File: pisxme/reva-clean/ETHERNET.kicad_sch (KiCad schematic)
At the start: 3 parts

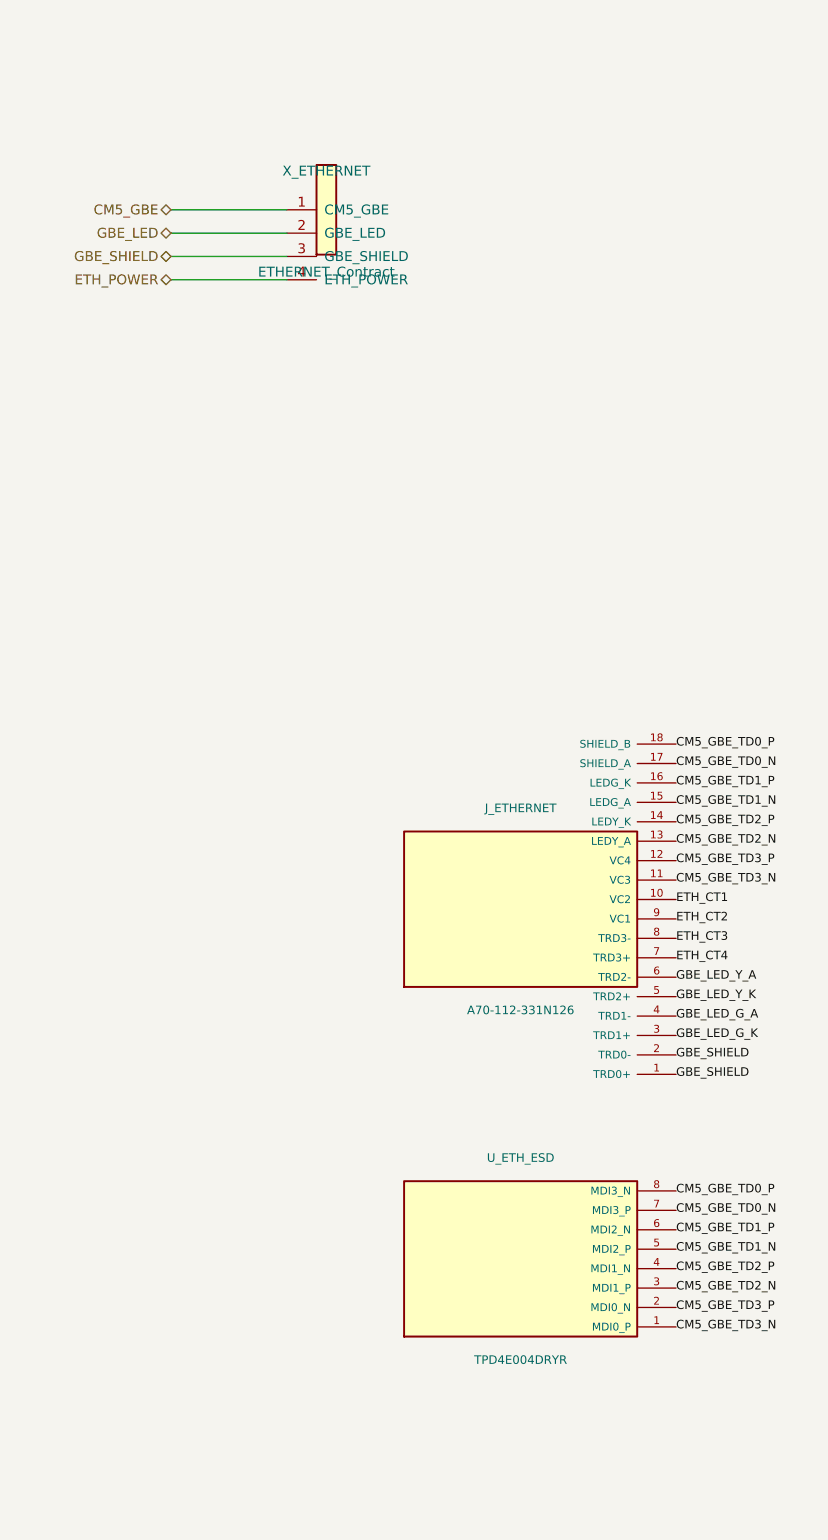
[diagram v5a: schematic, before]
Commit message: fix KiCad annotation and netlist export
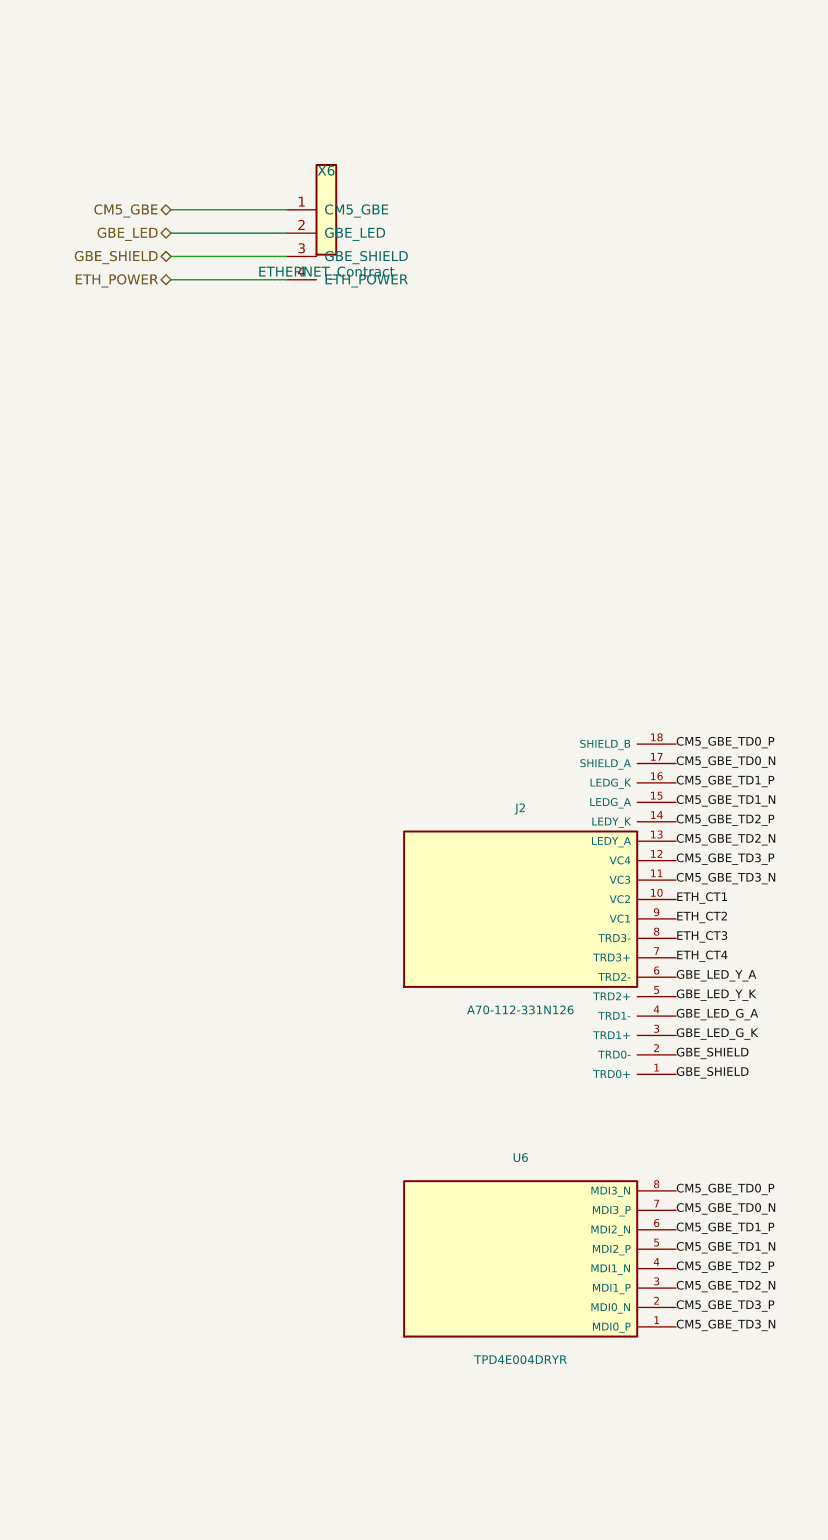
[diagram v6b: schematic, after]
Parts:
- renumbered J_ETHERNET to J2, U_ETH_ESD to U6, X_ETHERNET to X6
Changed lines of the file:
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@@
     (on_board no)
     (dnp no)
-    (property "Reference" "X_ETHERNET"
+    (property "Reference" "X6"
       (at 25 5 0)
       (effects (font (size 1.27 1.27))))
@@
     (pin "4")
     (instances (project "PiSXMe_RevA_Clean"
-      (path "/30000000-0000-0000-0000-000000000000/10000000-0000-0000-0000-000000000006" (reference "X_ETHERNET" ) (unit 1))))
+      (path "/30000000-0000-0000-0000-000000000000/10000000-0000-0000-0000-000000000006" (reference "X6" ) (unit 1))))
   )
 (label "CM5_GBE_TD0_P" (at 70 78.75 0) (effects (font (size 1.1 1.1)) (justify left)))
@@
 (label "GBE_SHIELD" (at 70 118.75 0) (effects (font (size 1.1 1.1)) (justify left)))
 (label "GBE_SHIELD" (at 70 121.25 0) (effects (font (size 1.1 1.1)) (justify left)))
-(symbol (lib_id "PiSXMeRevAClean:EDAC_A70_112_331N126_Ethernet") (at 50 100 0) (unit 1) (exclude_from_sim no) (in_bom yes) (on_board yes) (dnp no) (property "Reference" "J_ETHERNET" (at 50 87 0) (effects (font (size 1.1 1.1)))) (property "Value" "A70-112-331N126" (at 50 113 0) (effects (font (size 1.1 1.1)))) (property "MPN" "A70-112-331N126" (at 50 100 0) (effects (font (size 1 1)) (hide yes))) (property "Footprint" "PiSXMeRevAClean:EDAC_A70_112_331N126" (at 50 100 0) (effects (font (size 1 1)) (hide yes))) (pin "1")
+(symbol (lib_id "PiSXMeRevAClean:EDAC_A70_112_331N126_Ethernet") (at 50 100 0) (unit 1) (exclude_from_sim no) (in_bom yes) (on_board yes) (dnp no) (property "Reference" "J2" (at 50 87 0) (effects (font (size 1.1 1.1)))) (property "Value" "A70-112-331N126" (at 50 113 0) (effects (font (size 1.1 1.1)))) (property "MPN" "A70-112-331N126" (at 50 100 0) (effects (font (size 1 1)) (hide yes))) (property "Footprint" "PiSXMeRevAClean:EDAC_A70_112_331N126" (at 50 100 0) (effects (font (size 1 1)) (hide yes))) (pin "1")
 (pin "2")
 (pin "3")
@@
 (pin "16")
 (pin "17")
-(pin "18") (instances (project "PiSXMe_RevA_Clean" (path "/30000000-0000-0000-0000-000000000000" (reference "J_ETHERNET") (unit 1)))) )(label "CM5_GBE_TD0_P" (at 70 136.25 0) (effects (font (size 1.1 1.1)) (justify left)))
+(pin "18") (instances (project "PiSXMe_RevA_Clean" (path "/30000000-0000-0000-0000-000000000000" (reference "J2") (unit 1)))) )(label "CM5_GBE_TD0_P" (at 70 136.25 0) (effects (font (size 1.1 1.1)) (justify left)))
 (label "CM5_GBE_TD0_N" (at 70 138.75 0) (effects (font (size 1.1 1.1)) (justify left)))
 (label "CM5_GBE_TD1_P" (at 70 141.25 0) (effects (font (size 1.1 1.1)) (justify left)))
@@
 (label "CM5_GBE_TD3_P" (at 70 151.25 0) (effects (font (size 1.1 1.1)) (justify left)))
 (label "CM5_GBE_TD3_N" (at 70 153.75 0) (effects (font (size 1.1 1.1)) (justify left)))
-(symbol (lib_id "PiSXMeRevAClean:TPD4E004DRYR") (at 50 145 0) (unit 1) (exclude_from_sim no) (in_bom yes) (on_board yes) (dnp no) (property "Reference" "U_ETH_ESD" (at 50 132 0) (effects (font (size 1.1 1.1)))) (property "Value" "TPD4E004DRYR" (at 50 158 0) (effects (font (size 1.1 1.1)))) (property "MPN" "TPD4E004DRYR" (at 50 145 0) (effects (font (size 1 1)) (hide yes))) (property "Footprint" "PiSXMeRevAClean:TPD4E004DRYR_WSON6" (at 50 145 0) (effects (font (size 1 1)) (hide yes))) (pin "1")
+(symbol (lib_id "PiSXMeRevAClean:TPD4E004DRYR") (at 50 145 0) (unit 1) (exclude_from_sim no) (in_bom yes) (on_board yes) (dnp no) (property "Reference" "U6" (at 50 132 0) (effects (font (size 1.1 1.1)))) (property "Value" "TPD4E004DRYR" (at 50 158 0) (effects (font (size 1.1 1.1)))) (property "MPN" "TPD4E004DRYR" (at 50 145 0) (effects (font (size 1 1)) (hide yes))) (property "Footprint" "PiSXMeRevAClean:TPD4E004DRYR_WSON6" (at 50 145 0) (effects (font (size 1 1)) (hide yes))) (pin "1")
 (pin "2")
 (pin "3")
@@
 (pin "6")
 (pin "7")
-(pin "8") (instances (project "PiSXMe_RevA_Clean" (path "/30000000-0000-0000-0000-000000000000" (reference "U_ETH_ESD") (unit 1)))) )
+(pin "8") (instances (project "PiSXMe_RevA_Clean" (path "/30000000-0000-0000-0000-000000000000" (reference "U6") (unit 1)))) )
   (sheet_instances (path "/30000000-0000-0000-0000-000000000000/10000000-0000-0000-0000-000000000006" (page "6")))
 )

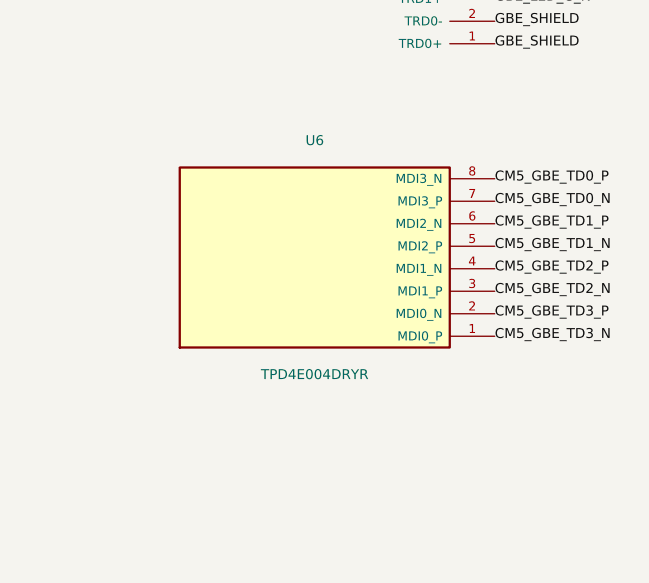
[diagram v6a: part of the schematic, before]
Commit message: correct Ethernet ESD and regulator authority
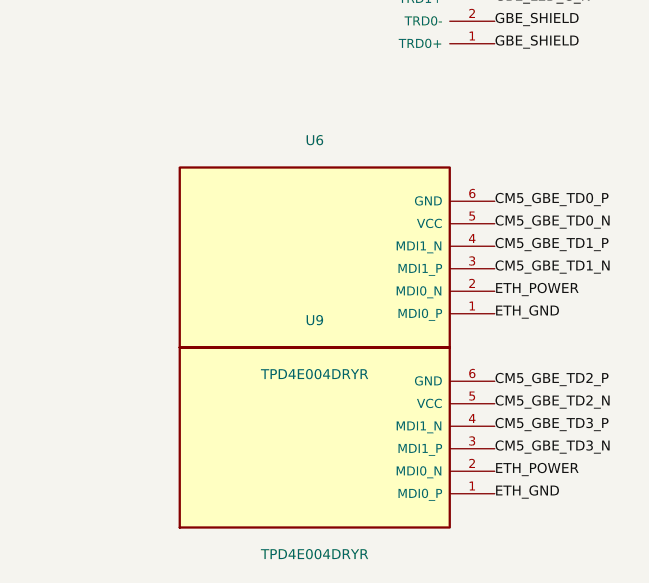
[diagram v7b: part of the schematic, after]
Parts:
- added U9: TPD4E004DRYR, PiSXMeRevAClean:TPD4E004DRYR_WSON6, symbol PiSXMeRevAClean:TPD4E004DRYR
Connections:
- net CM5_GBE_TD0_N: now also U6.5 (VCC); no longer U6.7 (MDI3_P)
- net CM5_GBE_TD0_P: now also U6.6 (GND); no longer U6.8 (MDI3_N)
- net CM5_GBE_TD1_N: now also U6.3 (MDI1_P); no longer U6.5 (MDI2_P)
- net CM5_GBE_TD1_P: now also U6.4 (MDI1_N); no longer U6.6 (MDI2_N)
- net CM5_GBE_TD2_N: now also U9.5 (VCC); no longer U6.3 (MDI1_P)
- net CM5_GBE_TD2_P: now also U9.6 (GND); no longer U6.4 (MDI1_N)
- net CM5_GBE_TD3_N: now also U9.3 (MDI1_P); no longer U6.1 (MDI0_P)
- net CM5_GBE_TD3_P: now also U9.4 (MDI1_N); no longer U6.2 (MDI0_N)
- net ETH_POWER: now also U6.2 (MDI0_N), U9.2 (MDI0_N)
- new net ETH_GND: U6.1 (MDI0_P), U9.1 (MDI0_P)
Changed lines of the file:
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@@
 (pin "16")
 (pin "17")
-(pin "18") (instances (project "PiSXMe_RevA_Clean" (path "/30000000-0000-0000-0000-000000000000" (reference "J2") (unit 1)))) )(label "CM5_GBE_TD0_P" (at 70 136.25 0) (effects (font (size 1.1 1.1)) (justify left)))
-(label "CM5_GBE_TD0_N" (at 70 138.75 0) (effects (font (size 1.1 1.1)) (justify left)))
-(label "CM5_GBE_TD1_P" (at 70 141.25 0) (effects (font (size 1.1 1.1)) (justify left)))
-(label "CM5_GBE_TD1_N" (at 70 143.75 0) (effects (font (size 1.1 1.1)) (justify left)))
-(label "CM5_GBE_TD2_P" (at 70 146.25 0) (effects (font (size 1.1 1.1)) (justify left)))
-(label "CM5_GBE_TD2_N" (at 70 148.75 0) (effects (font (size 1.1 1.1)) (justify left)))
-(label "CM5_GBE_TD3_P" (at 70 151.25 0) (effects (font (size 1.1 1.1)) (justify left)))
-(label "CM5_GBE_TD3_N" (at 70 153.75 0) (effects (font (size 1.1 1.1)) (justify left)))
+(pin "18") (instances (project "PiSXMe_RevA_Clean" (path "/30000000-0000-0000-0000-000000000000" (reference "J2") (unit 1)))) )
+(label "CM5_GBE_TD0_P" (at 70 138.75 0) (effects (font (size 1.1 1.1)) (justify left)))
+(label "CM5_GBE_TD0_N" (at 70 141.25 0) (effects (font (size 1.1 1.1)) (justify left)))
+(label "CM5_GBE_TD1_P" (at 70 143.75 0) (effects (font (size 1.1 1.1)) (justify left)))
+(label "CM5_GBE_TD1_N" (at 70 146.25 0) (effects (font (size 1.1 1.1)) (justify left)))
+(label "ETH_POWER" (at 70 148.75 0) (effects (font (size 1.1 1.1)) (justify left)))
+(label "ETH_GND" (at 70 151.25 0) (effects (font (size 1.1 1.1)) (justify left)))
 (symbol (lib_id "PiSXMeRevAClean:TPD4E004DRYR") (at 50 145 0) (unit 1) (exclude_from_sim no) (in_bom yes) (on_board yes) (dnp no) (property "Reference" "U6" (at 50 132 0) (effects (font (size 1.1 1.1)))) (property "Value" "TPD4E004DRYR" (at 50 158 0) (effects (font (size 1.1 1.1)))) (property "MPN" "TPD4E004DRYR" (at 50 145 0) (effects (font (size 1 1)) (hide yes))) (property "Footprint" "PiSXMeRevAClean:TPD4E004DRYR_WSON6" (at 50 145 0) (effects (font (size 1 1)) (hide yes))) (pin "1")
 (pin "2")
@@
 (pin "4")
 (pin "5")
-(pin "6")
-(pin "7")
-(pin "8") (instances (project "PiSXMe_RevA_Clean" (path "/30000000-0000-0000-0000-000000000000" (reference "U6") (unit 1)))) )
+(pin "6") (instances (project "PiSXMe_RevA_Clean" (path "/30000000-0000-0000-0000-000000000000" (reference "U6") (unit 1)))) )(label "CM5_GBE_TD2_P" (at 70 158.75 0) (effects (font (size 1.1 1.1)) (justify left)))
+(label "CM5_GBE_TD2_N" (at 70 161.25 0) (effects (font (size 1.1 1.1)) (justify left)))
+(label "CM5_GBE_TD3_P" (at 70 163.75 0) (effects (font (size 1.1 1.1)) (justify left)))
+(label "CM5_GBE_TD3_N" (at 70 166.25 0) (effects (font (size 1.1 1.1)) (justify left)))
+(label "ETH_POWER" (at 70 168.75 0) (effects (font (size 1.1 1.1)) (justify left)))
+(label "ETH_GND" (at 70 171.25 0) (effects (font (size 1.1 1.1)) (justify left)))
+(symbol (lib_id "PiSXMeRevAClean:TPD4E004DRYR") (at 50 165 0) (unit 1) (exclude_from_sim no) (in_bom yes) (on_board yes) (dnp no) (property "Reference" "U9" (at 50 152 0) (effects (font (size 1.1 1.1)))) (property "Value" "TPD4E004DRYR" (at 50 178 0) (effects (font (size 1.1 1.1)))) (property "MPN" "TPD4E004DRYR" (at 50 165 0) (effects (font (size 1 1)) (hide yes))) (property "Footprint" "PiSXMeRevAClean:TPD4E004DRYR_WSON6" (at 50 165 0) (effects (font (size 1 1)) (hide yes))) (pin "1")
+(pin "2")
+(pin "3")
+(pin "4")
+(pin "5")
+(pin "6") (instances (project "PiSXMe_RevA_Clean" (path "/30000000-0000-0000-0000-000000000000" (reference "U9") (unit 1)))) )
   (sheet_instances (path "/30000000-0000-0000-0000-000000000000/10000000-0000-0000-0000-000000000006" (page "6")))
 )
